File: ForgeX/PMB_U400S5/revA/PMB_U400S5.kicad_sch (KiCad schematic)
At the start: 26 parts, among them J1 Screw_Terminal_01x03, J10 Screw_Terminal_01x01, J11 Screw_Terminal_01x01, J12 Screw_Terminal_01x03, J13 Screw_Terminal_01x01, J14 Screw_Terminal_01x01, J15 Screw_Terminal_01x01, J16 Screw_Terminal_01x01, J17 Screw_Terminal_01x01, J18 Screw_Terminal_01x01, J2 Screw_Terminal_01x03, J3 Screw_Terminal_01x03, J4 Screw_Terminal_01x01, J5 Screw_Terminal_01x01, J6 Screw_Terminal_01x01, J7 Screw_Terminal_01x03, J8 Screw_Terminal_01x01, J9 Screw_Terminal_01x01

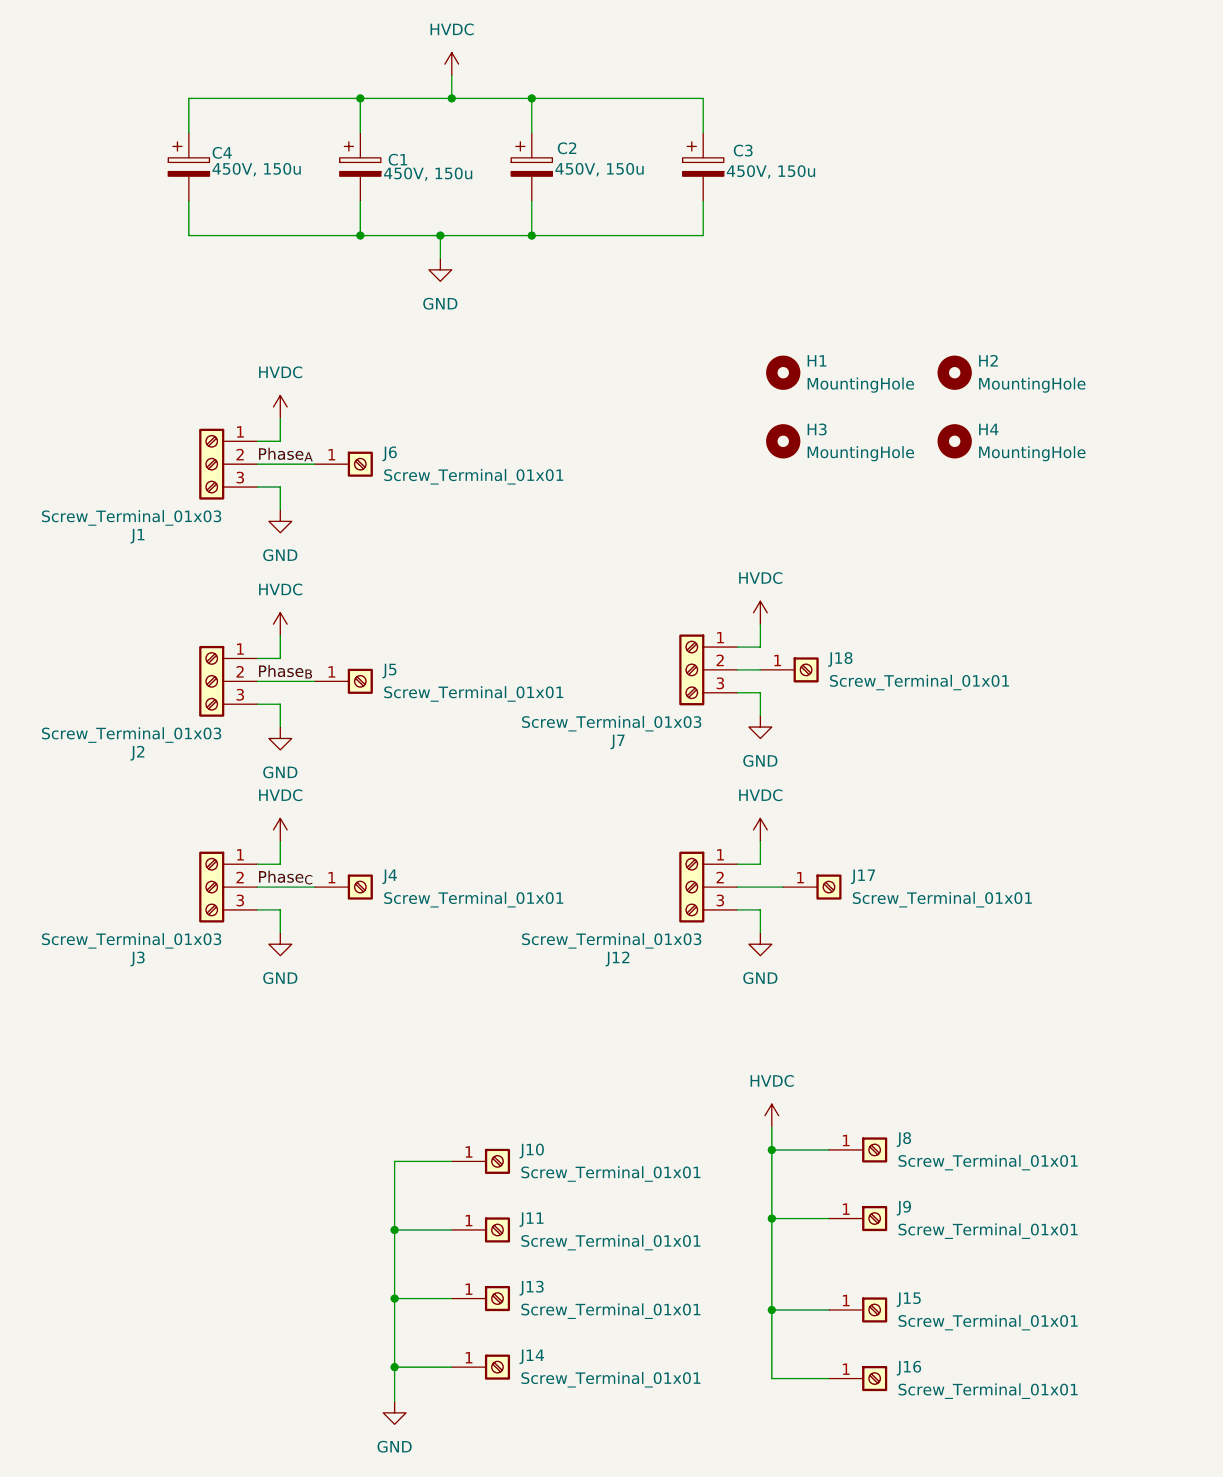
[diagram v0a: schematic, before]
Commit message: Major redesign & Reworks
* Star grounding scheme enforced across the whole ForgeX design....
* Viper26 based PSU designed
* Better signal integrity & decoupling on LVP and major reroute
* Laminated DC bus (Biplanar) , instead of (Coplanar) , for heavily reduced bus inductance & equivelant Electrolytics ESL
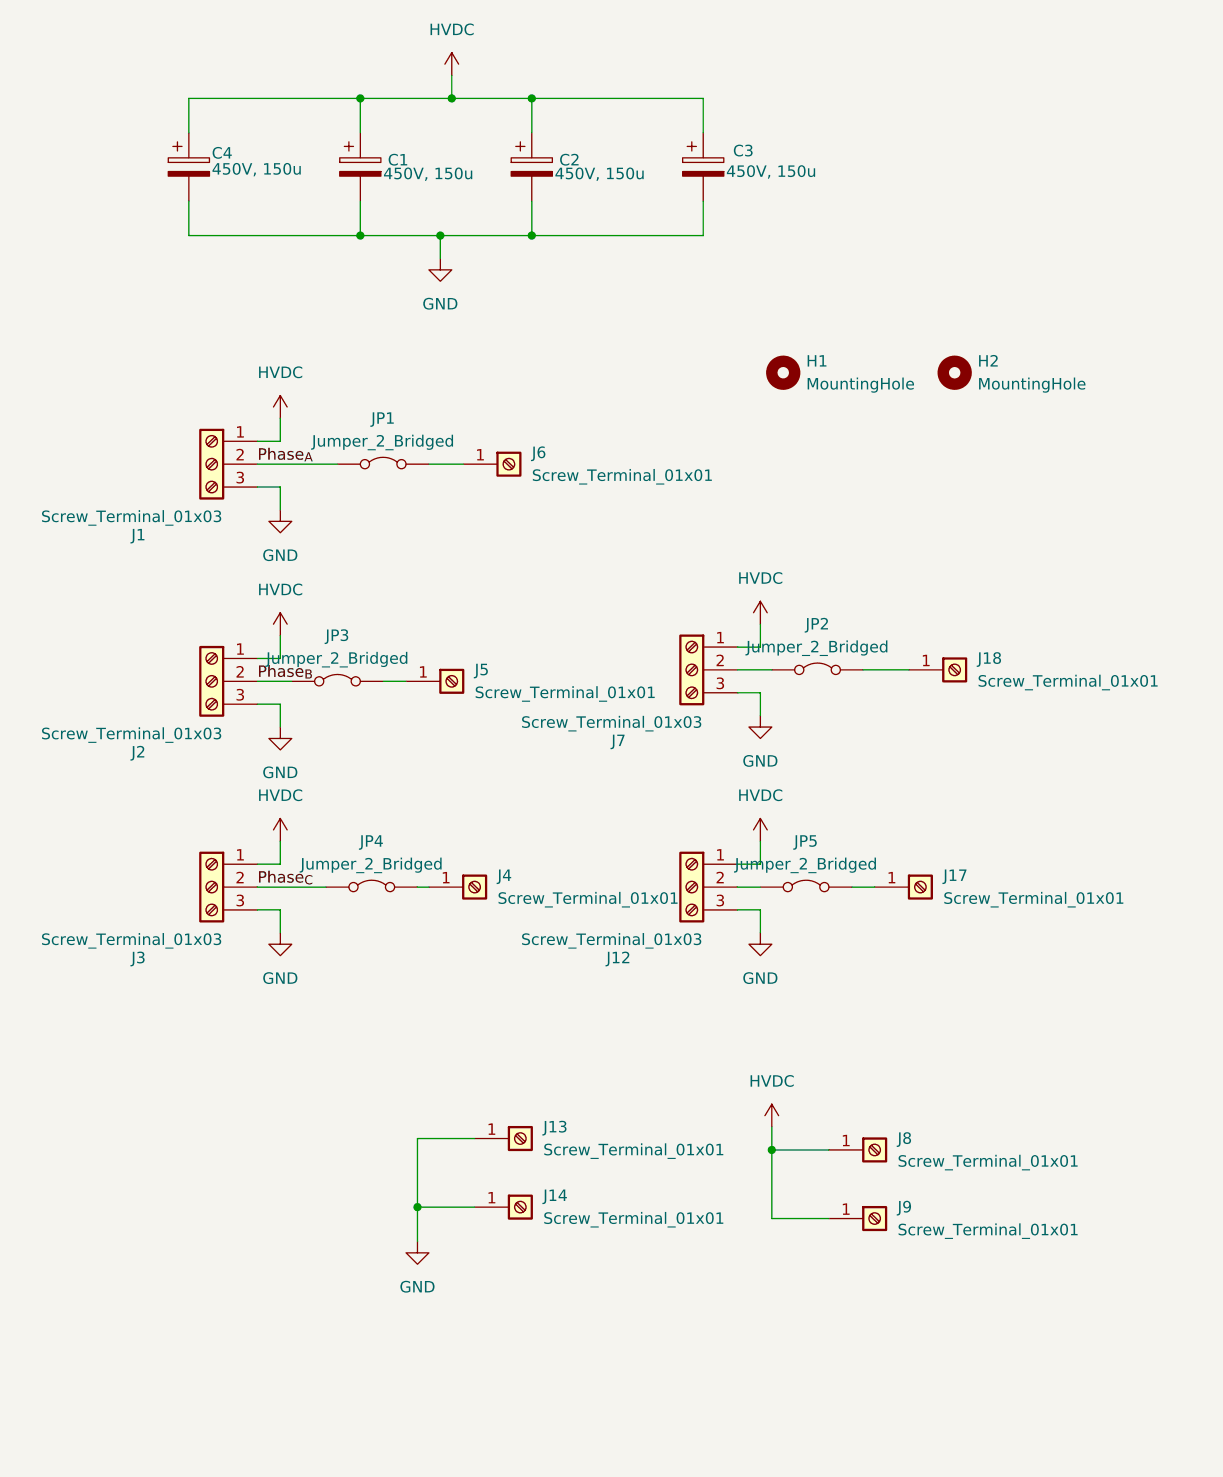
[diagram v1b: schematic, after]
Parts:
- removed H3, H4: MountingHole, MountingHole:MountingHole_5.3mm_M5_DIN965, symbol Mechanical:MountingHole
- removed J10, J11, J15, J16: Screw_Terminal_01x01, Libmain:M3_PCONN_1x01, symbol Connector:Screw_Terminal_01x01
- added JP1, JP2, JP3, JP4, JP5: Jumper_2_Bridged, Libmain:PowerJumper_PMB, symbol Jumper:Jumper_2_Bridged
- C1, C2, C3, C4: footprint Libmain:CP_Radial_D22.0mm_P10.00mm_SnapIn_Ceye -> Capacitor_THT:CP_Radial_D22.0mm_P10.00mm_SnapIn
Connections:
- net Phase_{A}: now also JP1.1 (A); no longer J6.1 (Pin_1)
- net Phase_{B}: now also JP3.1 (A); no longer J5.1 (Pin_1)
- net Phase_{C}: now also JP4.1 (A); no longer J4.1 (Pin_1)
- net at J17.1 (Pin_1): now also JP5.2 (B); no longer J12.2 (Pin_2)
- net at J7.2 (Pin_2): now also JP2.1 (A); no longer J18.1 (Pin_1)
- new net: J4.1 (Pin_1), JP4.2 (B)
- new net: J6.1 (Pin_1), JP1.2 (B)
- new net: J12.2 (Pin_2), JP5.1 (A)
- new net: J5.1 (Pin_1), JP3.2 (B)
- new net: J18.1 (Pin_1), JP2.2 (B)
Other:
- moved on the sheet: J13, J14, J17, J18, J4, J5, J6
